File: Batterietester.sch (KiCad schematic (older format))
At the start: 16 parts, among them J1 CONN_01X02, J2 CONN_01X02, J3 CONN_01X02, J4 CONN_01X02, SW1 SW_Push, SW2 SW_Push, U1 LM3914

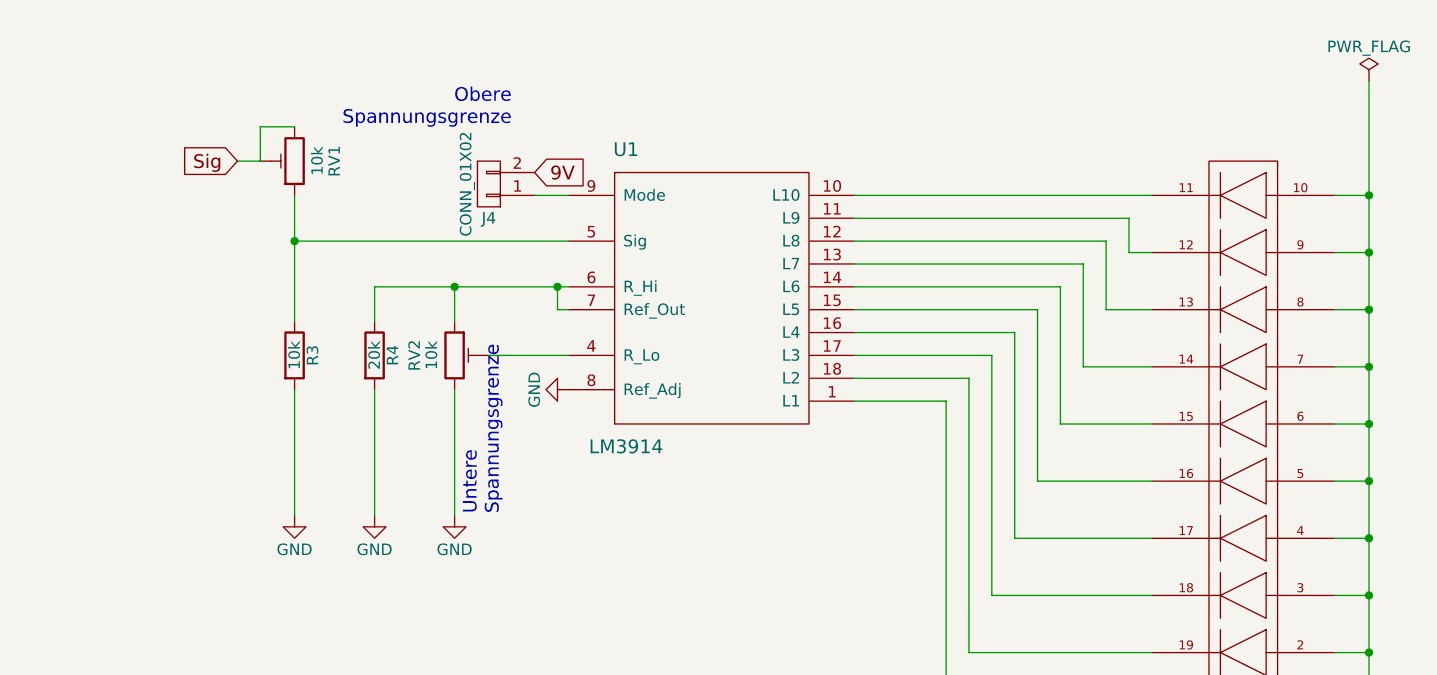
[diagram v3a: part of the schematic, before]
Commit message: changed variable resistors
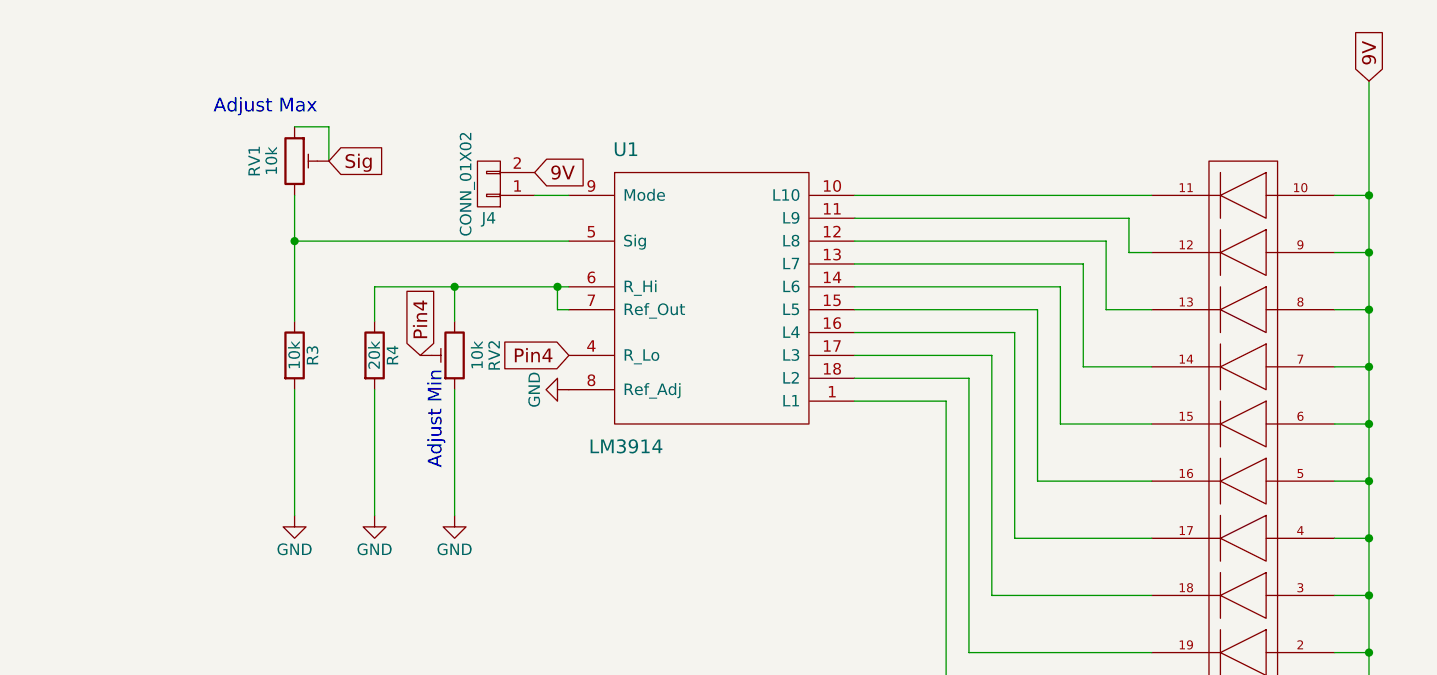
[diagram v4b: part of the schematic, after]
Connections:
- net GND: now also RV2.1; no longer RV2.3
- net Sig: now also RV1.1; no longer RV1.3
- net VCC: now also BAR1.1 (A), BAR1.10 (A), BAR1.2 (A), BAR1.3 (A), BAR1.4 (A), BAR1.5 (A), BAR1.6 (A), BAR1.7 (A), BAR1.8 (A), BAR1.9 (A)
- net at R3.1, U1.5 (Sig): now also RV1.3; no longer RV1.1
- net at R4.1, U1.6 (R_Hi), U1.7 (Ref_Out): now also RV2.3; no longer RV2.1
- net Pin4: now reaches RV2.2, U1.4 (R_Lo)
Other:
- note added: "Adjust Max"
- note added: "Adjust Min"
- note removed: "Obere\nSpannungsgrenze"
- note removed: "Untere\nSpannungsgrenze"
- moved on the sheet: RV1, RV2
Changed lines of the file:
@@
-$EndComp
-$Comp
-L PWR_FLAG #FLG03
-U 1 1 59FF3941
-P 10850 1300
-F 0 "#FLG03" H 10850 1375 50  0001 C CNN
-F 1 "PWR_FLAG" H 10850 1450 50  0000 C CNN
-F 2 "" H 10850 1300 50  0001 C CNN
-F 3 "" H 10850 1300 50  0001 C CNN
-	1    10850 1300
-	1    0    0    -1
 $EndComp
 $Comp
@@
 $EndComp
 $Comp
-L GND #PWR04
+L GND #PWR03
 U 1 1 59FF35E5
 P 6500 3200
-F 0 "#PWR04" H 6500 2950 50  0001 C CNN
+F 0 "#PWR03" H 6500 2950 50  0001 C CNN
 F 1 "GND" H 6500 3050 50  0000 C CNN
 F 2 "" H 6500 3200 50  0001 C CNN
@@
 $EndComp
 $Comp
-L GND #PWR05
+L GND #PWR04
 U 1 1 59FF3605
 P 6150 3200
-F 0 "#PWR05" H 6150 2950 50  0001 C CNN
+F 0 "#PWR04" H 6150 2950 50  0001 C CNN
 F 1 "GND" H 6150 3050 50  0000 C CNN
 F 2 "" H 6150 3200 50  0001 C CNN
@@
 F 3 "" H 6150 1650 50  0001 C CNN
 	1    6150 1650
-	-1   0    0    1
+	1    0    0    -1
 $EndComp
 $Comp
@@
 F 3 "" H 6850 2500 50  0001 C CNN
 	1    6850 2500
-	1    0    0    -1
-$EndComp
-$Comp
-L GND #PWR06
+	-1   0    0    1
+$EndComp
+$Comp
+L GND #PWR05
 U 1 1 59FF3C15
 P 6850 3200
-F 0 "#PWR06" H 6850 2950 50  0001 C CNN
+F 0 "#PWR05" H 6850 2950 50  0001 C CNN
 F 1 "GND" H 6850 3050 50  0000 C CNN
 F 2 "" H 6850 3200 50  0001 C CNN
@@
 $EndComp
 $Comp
-L GND #PWR07
+L GND #PWR06
 U 1 1 59FF46B3
 P 7350 2650
-F 0 "#PWR07" H 7350 2400 50  0001 C CNN
+F 0 "#PWR06" H 7350 2400 50  0001 C CNN
 F 1 "GND" H 7350 2500 50  0000 C CNN
 F 2 "" H 7350 2650 50  0001 C CNN
@@
 	0    1    1    0
 $EndComp
-Text Notes 7050 3200 1    60   ~ 0
-Untere\nSpannungsgrenze
-Text Notes 7100 1500 2    60   ~ 0
-Obere\nSpannungsgrenze
+Text Notes 6800 3000 1    60   ~ 0
+Adjust Min
+Text Notes 6250 1450 2    60   ~ 0
+Adjust Max
 $Comp
 L R R1
@@
 $EndComp
 $Comp
-L GND #PWR08
+L GND #PWR07
 U 1 1 59FF4FB8
 P 1900 4300
-F 0 "#PWR08" H 1900 4050 50  0001 C CNN
+F 0 "#PWR07" H 1900 4050 50  0001 C CNN
 F 1 "GND" H 1900 4150 50  0000 C CNN
 F 2 "" H 1900 4300 50  0001 C CNN
@@
 Text GLabel 1450 3300 0    60   Input ~ 0
 Sig
-Text GLabel 5900 1650 0    60   Input ~ 0
-Sig
-$Comp
-L GND #PWR09
+$Comp
+L GND #PWR08
 U 1 1 59FF568B
 P 2300 2700
-F 0 "#PWR09" H 2300 2450 50  0001 C CNN
+F 0 "#PWR08" H 2300 2450 50  0001 C CNN
 F 1 "GND" H 2300 2550 50  0000 C CNN
 F 2 "" H 2300 2700 50  0001 C CNN
@@
 $EndComp
 $Comp
-L PWR_FLAG #FLG010
+L PWR_FLAG #FLG09
 U 1 1 5A00B5E3
 P 2350 2650
-F 0 "#FLG010" H 2350 2725 50  0001 C CNN
+F 0 "#FLG09" H 2350 2725 50  0001 C CNN
 F 1 "PWR_FLAG" H 2350 2800 50  0000 C CNN
 F 2 "" H 2350 2650 50  0001 C CNN
@@
 $EndComp
 $Comp
-L VCC #PWR011
+L VCC #PWR010
 U 1 1 5A00B84A
 P 2950 1750
-F 0 "#PWR011" H 2950 1600 50  0001 C CNN
+F 0 "#PWR010" H 2950 1600 50  0001 C CNN
 F 1 "VCC" H 2950 1900 50  0000 C CNN
 F 2 "" H 2950 1750 50  0001 C CNN
@@
 $EndComp
 $Comp
-L GND #PWR012
+L GND #PWR011
 U 1 1 5A060BBC
 P 3750 1900
-F 0 "#PWR012" H 3750 1650 50  0001 C CNN
+F 0 "#PWR011" H 3750 1650 50  0001 C CNN
 F 1 "GND" H 3750 1750 50  0000 C CNN
 F 2 "" H 3750 1900 50  0001 C CNN
@@
 	0    -1   -1   0
 $EndComp
-Wire Wire Line
-	7350 1800 7200 1800
-Wire Wire Line
-	1450 3300 1600 3300
-Wire Wire Line
-	2150 3300 2000 3300
-Wire Wire Line
-	6000 1650 6000 1500
-Wire Wire Line
-	5900 1650 6000 1650
-Wire Wire Line
-	6000 1500 6150 1500
-Wire Wire Line
-	1500 4300 1500 4100
-Wire Wire Line
-	1900 4200 1900 4300
-Wire Wire Line
-	1500 3800 1500 4000
-Wire Wire Line
-	1900 3900 1900 3800
-Wire Wire Line
-	7300 2200 7300 2300
-Connection ~ 6850 2200
-Wire Wire Line
-	7300 2300 7350 2300
-Connection ~ 7300 2200
-Wire Wire Line
-	6500 2200 6500 2350
-Wire Wire Line
-	6850 2200 6850 2350
-Wire Wire Line
-	7000 2500 7350 2500
-Wire Wire Line
-	6850 2650 6850 3200
-Connection ~ 6150 2000
-Wire Wire Line
-	6150 1800 6150 2350
-Wire Wire Line
-	6150 2000 7350 2000
-Wire Wire Line
-	6150 2650 6150 3200
-Wire Wire Line
-	6500 2650 6500 3200
-Wire Wire Line
-	6500 2200 7350 2200
-Wire Wire Line
-	2750 2350 3150 2350
-Connection ~ 10850 3800
-Wire Wire Line
-	10850 3800 10700 3800
-Connection ~ 10850 3550
-Wire Wire Line
-	10850 3550 10700 3550
-Connection ~ 10850 3300
-Wire Wire Line
-	10850 3300 10700 3300
-Connection ~ 10850 3050
-Wire Wire Line
-	10850 3050 10700 3050
-Connection ~ 10850 2800
-Wire Wire Line
-	10850 2800 10700 2800
-Connection ~ 10850 2550
-Wire Wire Line
-	10850 2550 10700 2550
-Connection ~ 10850 2300
-Wire Wire Line
-	10850 2300 10700 2300
-Connection ~ 10850 2050
-Wire Wire Line
-	10850 2050 10700 2050
-Connection ~ 10850 1800
-Wire Wire Line
-	10700 1800 10850 1800
-Wire Wire Line
-	10850 1300 10850 4050
-Wire Wire Line
-	10850 4050 10700 4050
-Wire Wire Line
-	9000 4050 9900 4050
-Wire Wire Line
-	9000 2700 9000 4050
-Wire Wire Line
-	8600 2700 9000 2700
-Wire Wire Line
-	9100 3800 9900 3800
-Wire Wire Line
-	9100 2600 9100 3800
-Wire Wire Line
-	8600 2600 9100 2600
-Wire Wire Line
-	9200 3550 9900 3550
-Wire Wire Line
-	9200 2500 9200 3550
-Wire Wire Line
-	8600 2500 9200 2500
-Wire Wire Line
-	9300 3300 9900 3300
-Wire Wire Line
-	9300 2400 9300 3300
-Wire Wire Line
-	8600 2400 9300 2400
-Wire Wire Line
-	9400 3050 9900 3050
-Wire Wire Line
-	9400 2300 9400 3050
-Wire Wire Line
-	8600 2300 9400 2300
-Wire Wire Line
-	9500 2800 9900 2800
-Wire Wire Line
-	9500 2200 9500 2800
-Wire Wire Line
-	8600 2200 9500 2200
-Wire Wire Line
-	9600 2550 9900 2550
-Wire Wire Line
-	9600 2100 9600 2550
-Wire Wire Line
-	8600 2100 9600 2100
-Wire Wire Line
-	9700 2300 9900 2300
-Wire Wire Line
-	9700 2000 9700 2300
-Wire Wire Line
-	8600 2000 9700 2000
-Wire Wire Line
-	9800 2050 9900 2050
-Wire Wire Line
-	9800 1900 9800 2050
-Wire Wire Line
-	8600 1900 9800 1900
-Wire Wire Line
-	9900 1800 8600 1800
-Wire Wire Line
-	2300 2450 2300 2700
-Wire Wire Line
-	2350 2650 2300 2650
-Connection ~ 2300 2650
-Wire Wire Line
-	2300 2350 2350 2350
-Wire Wire Line
-	3150 1900 2950 1900
-Wire Wire Line
-	2950 1750 2950 2350
-Connection ~ 2950 1900
-Connection ~ 1900 4300
-Connection ~ 1900 3800
-Wire Wire Line
-	2450 4100 2250 4100
-Wire Wire Line
-	2250 4100 2250 3800
-Wire Wire Line
-	2250 3800 1500 3800
-Wire Wire Line
-	2450 4300 2450 4000
-Wire Wire Line
-	1500 4300 2450 4300
-Connection ~ 2950 2350
 $Comp
 L CONN_01X02 J4
@@
 	1    0    0    -1
 $EndComp
+Text GLabel 10850 1300 1    60   Input ~ 0
+9V
+Text GLabel 7350 2500 0    60   Input ~ 0
+Pin4
+Text GLabel 6700 2500 1    60   Input ~ 0
+Pin4
+Wire Wire Line
+	7350 1800 7200 1800
+Wire Wire Line
+	1450 3300 1600 3300
+Wire Wire Line
+	2150 3300 2000 3300
+Wire Wire Line
+	1500 4300 1500 4100
+Wire Wire Line
+	1900 4200 1900 4300
+Wire Wire Line
+	1500 3800 1500 4000
+Wire Wire Line
+	1900 3900 1900 3800
+Wire Wire Line
+	7300 2200 7300 2300
+Connection ~ 6850 2200
+Wire Wire Line
+	7300 2300 7350 2300
+Connection ~ 7300 2200
+Wire Wire Line
+	6500 2200 6500 2350
+Wire Wire Line
+	6850 2200 6850 2350
+Wire Wire Line
+	6850 2650 6850 3200
+Connection ~ 6150 2000
+Wire Wire Line
+	6150 1800 6150 2350
+Wire Wire Line
+	6150 2000 7350 2000
+Wire Wire Line
+	6150 2650 6150 3200
+Wire Wire Line
+	6500 2650 6500 3200
+Wire Wire Line
+	6500 2200 7350 2200
+Wire Wire Line
+	2750 2350 3150 2350
+Connection ~ 10850 3800
+Wire Wire Line
+	10850 3800 10700 3800
+Connection ~ 10850 3550
+Wire Wire Line
+	10850 3550 10700 3550
+Connection ~ 10850 3300
+Wire Wire Line
+	10850 3300 10700 3300
+Connection ~ 10850 3050
+Wire Wire Line
+	10850 3050 10700 3050
+Connection ~ 10850 2800
+Wire Wire Line
+	10850 2800 10700 2800
+Connection ~ 10850 2550
+Wire Wire Line
+	10850 2550 10700 2550
+Connection ~ 10850 2300
+Wire Wire Line
+	10850 2300 10700 2300
+Connection ~ 10850 2050
+Wire Wire Line
+	10850 2050 10700 2050
+Connection ~ 10850 1800
+Wire Wire Line
+	10700 1800 10850 1800
+Wire Wire Line
+	10850 1300 10850 4050
+Wire Wire Line
+	10850 4050 10700 4050
+Wire Wire Line
+	9000 4050 9900 4050
+Wire Wire Line
+	9000 2700 9000 4050
+Wire Wire Line
+	8600 2700 9000 2700
+Wire Wire Line
+	9100 3800 9900 3800
+Wire Wire Line
+	9100 2600 9100 3800
+Wire Wire Line
+	8600 2600 9100 2600
+Wire Wire Line
+	9200 3550 9900 3550
+Wire Wire Line
+	9200 2500 9200 3550
+Wire Wire Line
+	8600 2500 9200 2500
+Wire Wire Line
+	9300 3300 9900 3300
+Wire Wire Line
+	9300 2400 9300 3300
+Wire Wire Line
+	8600 2400 9300 2400
+Wire Wire Line
+	9400 3050 9900 3050
+Wire Wire Line
+	9400 2300 9400 3050
+Wire Wire Line
+	8600 2300 9400 2300
+Wire Wire Line
+	9500 2800 9900 2800
+Wire Wire Line
+	9500 2200 9500 2800
+Wire Wire Line
+	8600 2200 9500 2200
+Wire Wire Line
+	9600 2550 9900 2550
+Wire Wire Line
+	9600 2100 9600 2550
+Wire Wire Line
+	8600 2100 9600 2100
+Wire Wire Line
+	9700 2300 9900 2300
+Wire Wire Line
+	9700 2000 9700 2300
+Wire Wire Line
+	8600 2000 9700 2000
+Wire Wire Line
+	9800 2050 9900 2050
+Wire Wire Line
+	9800 1900 9800 2050
+Wire Wire Line
+	8600 1900 9800 1900
+Wire Wire Line
+	9900 1800 8600 1800
+Wire Wire Line
+	2300 2450 2300 2700
+Wire Wire Line
+	2350 2650 2300 2650
+Connection ~ 2300 2650
+Wire Wire Line
+	2300 2350 2350 2350
+Wire Wire Line
+	3150 1900 2950 1900
+Wire Wire Line
+	2950 1750 2950 2350
+Connection ~ 2950 1900
+Connection ~ 1900 4300
+Connection ~ 1900 3800
+Wire Wire Line
+	2450 4100 2250 4100
+Wire Wire Line
+	2250 4100 2250 3800
+Wire Wire Line
+	2250 3800 1500 3800
+Wire Wire Line
+	2450 4300 2450 4000
+Wire Wire Line
+	1500 4300 2450 4300
+Connection ~ 2950 2350
+Wire Wire Line
+	6300 1650 6300 1500
+Wire Wire Line
+	6300 1500 6150 1500
+Text GLabel 6300 1650 2    60   Input ~ 0
+Sig
 $EndSCHEMATC

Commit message: change layout
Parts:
- RV1, RV2: footprint Potentiometers:Potentiometer_Trimmer_ACP_CA6v_Horizontal -> Potentiometers:Potentiometer_Trimmer_Copal_CT-6EP
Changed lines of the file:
@@
 Title "Batterietester"
 Date "2017-11-05"
-Rev "1"
+Rev "2"
 Comp "Andreas Böttger"
 Comment1 "Batterietester für AA und AAA"
@@
 F 0 "RV1" V 5975 1650 50  0000 C CNN
 F 1 "10k" V 6050 1650 50  0000 C CNN
-F 2 "Potentiometers:Potentiometer_Trimmer_ACP_CA6v_Horizontal" H 6150 1650 50  0001 C CNN
+F 2 "Potentiometers:Potentiometer_Trimmer_Copal_CT-6EP" H 6150 1650 50  0001 C CNN
 F 3 "" H 6150 1650 50  0001 C CNN
 	1    6150 1650
@@
 F 0 "RV2" V 6675 2500 50  0000 C CNN
 F 1 "10k" V 6750 2500 50  0000 C CNN
-F 2 "Potentiometers:Potentiometer_Trimmer_ACP_CA6v_Horizontal" H 6850 2500 50  0001 C CNN
+F 2 "Potentiometers:Potentiometer_Trimmer_Copal_CT-6EP" H 6850 2500 50  0001 C CNN
 F 3 "" H 6850 2500 50  0001 C CNN
 	1    6850 2500

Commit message: cleaning
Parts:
- removed J1, J2, J3: CONN_01X02, Pin_Headers:Pin_Header_Angled_1x02_Pitch2.54mm, symbol CONN_01X02
- added J1, J2, J3: Screw_Terminal_1x02, TerminalBlock_Phoenix:TerminalBlock_Phoenix_MKDS1.5-2pol, symbol Screw_Terminal_1x02
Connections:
- net GND: now also R1.1, J1.1, J2.1, J3.1; no longer R1.2
- net SW_L: now also R1.2, J2.2, J3.2; no longer R1.1
- net at SW2.1: now also J1.2
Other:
- moved on the sheet: C1, D1, R1, R2, SW2

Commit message: correct capacitor
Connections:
- net GND: now also C1.2; no longer C1.1
- net VCC: now also C1.1; no longer C1.2
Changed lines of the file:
@@
 F 3 "" H 2750 2200 50  0001 C CNN
 	1    2750 2200
-	0    1    1    0
+	0    -1   -1   0
 $EndComp
 $Comp

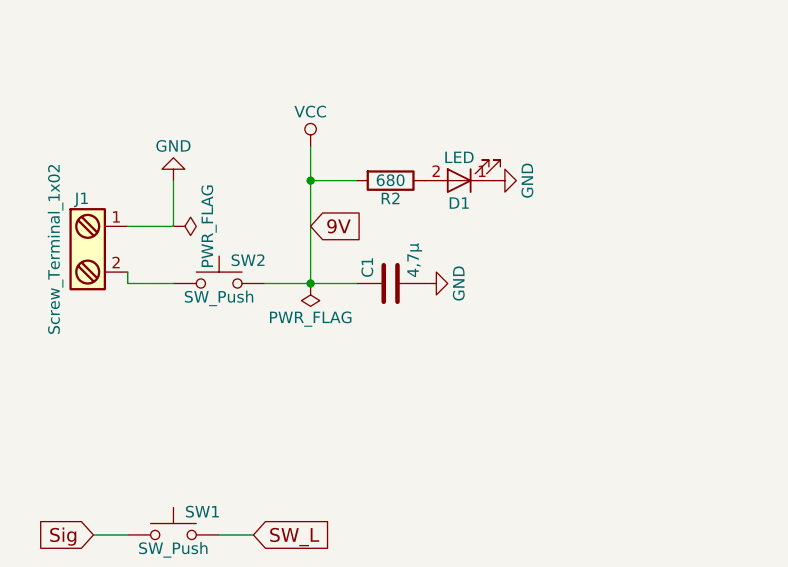
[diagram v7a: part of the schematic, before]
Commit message: use polarized capacitor
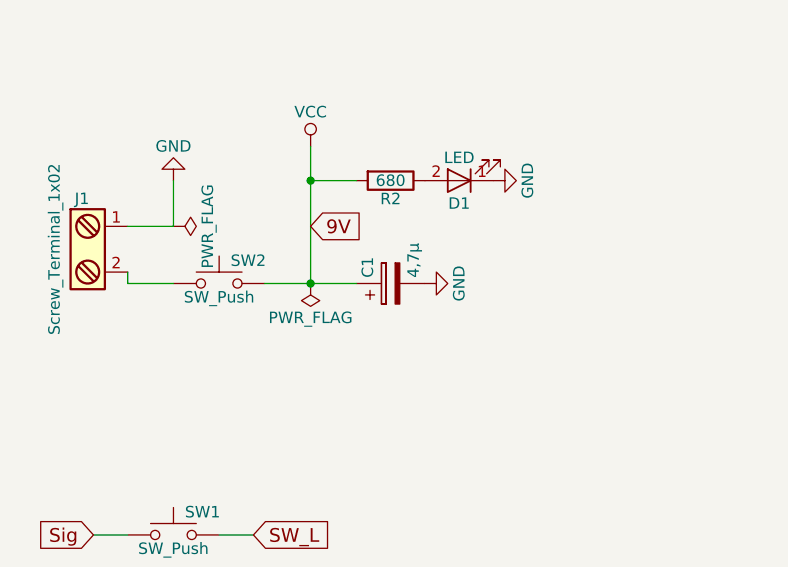
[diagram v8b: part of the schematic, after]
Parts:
- removed C1: 4,7µ, Capacitors_ThroughHole:CP_Radial_D4.0mm_P1.50mm, symbol C
- added C1: 4,7µ, Capacitors_ThroughHole:CP_Radial_D4.0mm_P1.50mm, symbol CP
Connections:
- net GND: now also C1.2
- net VCC: now also C1.1
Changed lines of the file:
@@
-$EndComp
-$Comp
-L C C1
-U 1 1 59FF1D94
-P 2750 2200
-F 0 "C1" H 2775 2300 50  0000 L CNN
-F 1 "4,7µ" H 2775 2100 50  0000 L CNN
-F 2 "Capacitors_ThroughHole:CP_Radial_D4.0mm_P1.50mm" H 2788 2050 50  0001 C CNN
-F 3 "" H 2750 2200 50  0001 C CNN
-	1    2750 2200
-	0    -1   -1   0
 $EndComp
 $Comp
@@
 	0    1    1    0
 $EndComp
+$Comp
+L CP C1
+U 1 1 5A21BB0E
+P 2750 2200
+F 0 "C1" H 2775 2300 50  0000 L CNN
+F 1 "4,7µ" H 2775 2100 50  0000 L CNN
+F 2 "Capacitors_ThroughHole:CP_Radial_D4.0mm_P1.50mm" H 2788 2050 50  0001 C CNN
+F 3 "" H 2750 2200 50  0001 C CNN
+	1    2750 2200
+	0    -1   -1   0
+$EndComp
 $EndSCHEMATC
